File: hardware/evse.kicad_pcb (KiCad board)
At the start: 2 copper layers, 42.5 x 62.5 mm, 87 parts, among them J101 Boot, P101 CON-SENSOR2, P102 Relay, P104 12V/Motor/GP, P105 CP/PP/PE, U101 XMC1100, U102 PEM1-S12-D12-S, U103 MAX14850, U104 ADS1118I, U105 OPA171AIDBV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

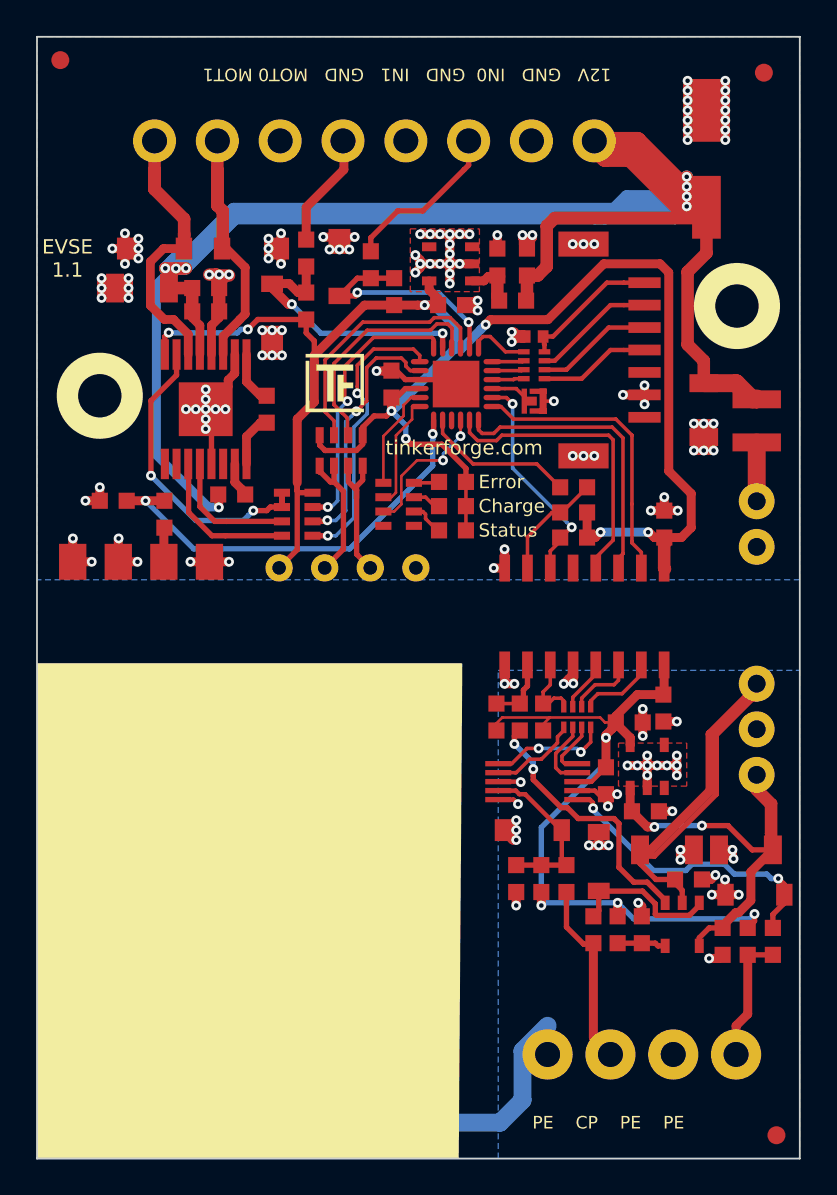
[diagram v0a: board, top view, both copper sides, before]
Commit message: fix tvs/zener diodes, fix pp description
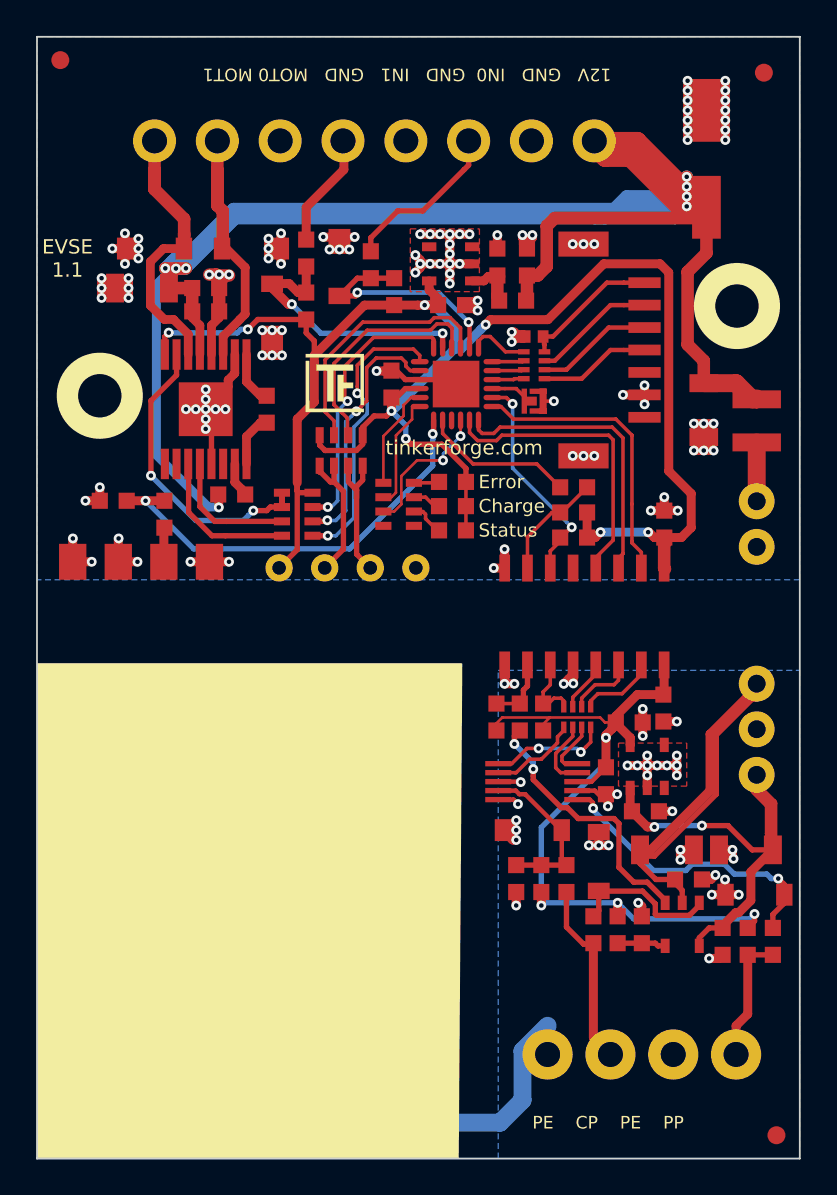
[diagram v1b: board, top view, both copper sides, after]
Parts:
- turned D104 to 270 degrees
- turned D106 to 180 degrees
- turned D107 to 180 degrees
- turned D110 to 90 degrees
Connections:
- D104 pad 1: INPUT-MOTOR-SWITCH -> GND
- D104 pad 2: GND -> INPUT-MOTOR-SWITCH
- D106 pad 1: Net-(D106-Pad1) -> AGND
- D106 pad 2: AGND -> Net-(D106-Pad2)
- D107 pad 1: Net-(D107-Pad1) -> AGND
- D107 pad 2: AGND -> Net-(D107-Pad2)
- D110 pad 1: INPUT-GP -> GND
- D110 pad 2: GND -> INPUT-GP
- R108 pad 1: Net-(D106-Pad1) -> Net-(D106-Pad2)
- R109 pad 1: Net-(D106-Pad1) -> Net-(D106-Pad2)
- R110 pad 2: Net-(D106-Pad1) -> Net-(D106-Pad2)
- R112 pad 2: Net-(D107-Pad1) -> Net-(D107-Pad2)
- U104 pad 4: Net-(D106-Pad1) -> Net-(D106-Pad2)
- U104 pad 6: Net-(D107-Pad1) -> Net-(D107-Pad2)
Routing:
- net Net-(D107-Pad2): track 0.00 -> 16.7 mm, vias 0 -> 2
- net Net-(D107-Pad1): track 16.7 -> 0.00 mm, vias 2 -> 0
- net Net-(D106-Pad2): track 0.00 -> 9.22 mm
- net Net-(D106-Pad1): track 9.22 -> 0.00 mm
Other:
- board text added: "PE CP PE PP"
- board text removed: "PE CP PE PE"

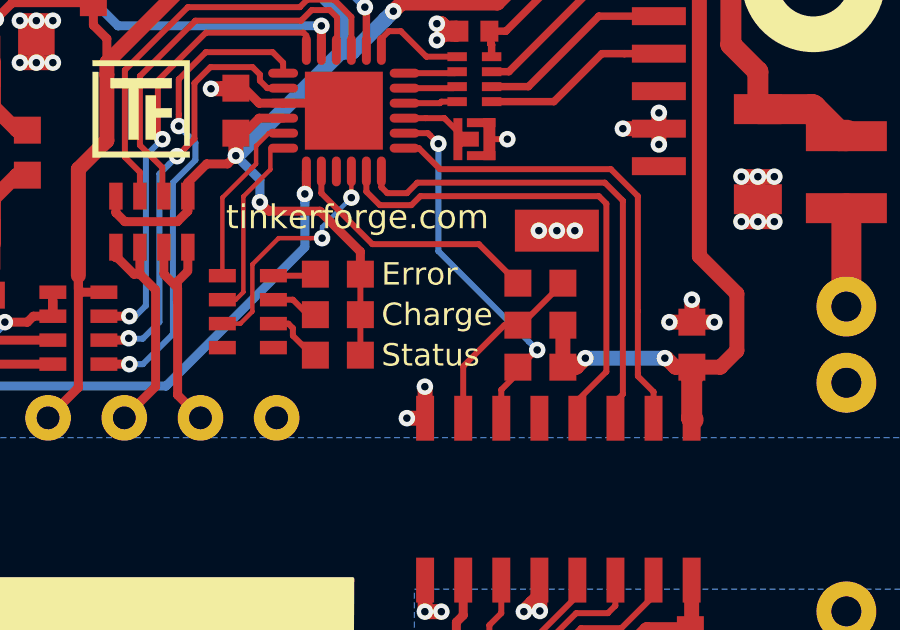
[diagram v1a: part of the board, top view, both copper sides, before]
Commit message: fix led colors and description
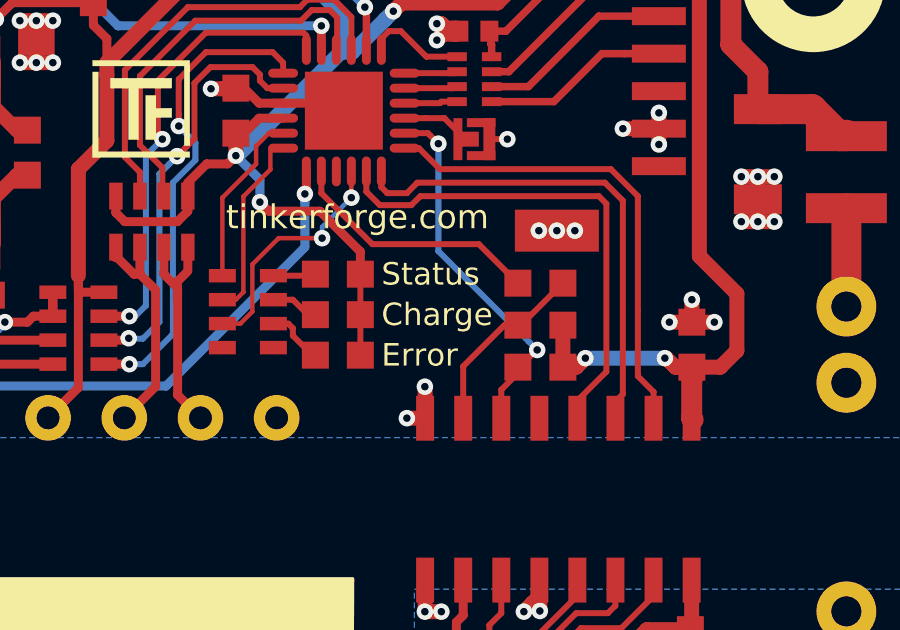
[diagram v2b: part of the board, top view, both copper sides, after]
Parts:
- D101: value blue -> red
- D103: value red -> blue
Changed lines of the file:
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@@
       (effects (font (size 0.2 0.2) (thickness 0.05)))
     )
-    (fp_text value blue (at 0.75 0.45) (layer F.Fab)
+    (fp_text value red (at 0.75 0.45) (layer F.Fab)
       (effects (font (size 0.2 0.2) (thickness 0.05)))
     )
@@
       (effects (font (size 0.2 0.2) (thickness 0.05)))
     )
-    (fp_text value red (at 0.75 0.45) (layer F.Fab)
+    (fp_text value blue (at 0.75 0.45) (layer F.Fab)
       (effects (font (size 0.2 0.2) (thickness 0.05)))
     )
@@
     (effects (font (size 0.8 0.8) (thickness 0.15)))
   )
-  (gr_text Error (at 163.6 81.95) (layer F.SilkS)
+  (gr_text Status (at 163.6 81.95) (layer F.SilkS)
     (effects (font (size 0.75 0.75) (thickness 0.15)) (justify left))
   )
@@
     (effects (font (size 0.75 0.75) (thickness 0.15)) (justify left))
   )
-  (gr_text Status (at 163.6 84.65) (layer F.SilkS)
+  (gr_text Error (at 163.6 84.65) (layer F.SilkS)
     (effects (font (size 0.75 0.75) (thickness 0.15)) (justify left))
   )
@@
   (segment (start 175.89996 105.55098) (end 175.350769 106.100171) (width 0.3) (layer F.Cu) (net 60))
   (segment (start 172.738202 104.75) (end 170.3 104.75) (width 0.3) (layer F.Cu) (net 60))
-  (segment (start 168.2383 101.35) (end 168.2383 102.9883) (width 0.25) (layer F.Cu) (net 87))
-  (segment (start 168.2383 102.9883) (end 168.5 103.25) (width 0.25) (layer F.Cu) (net 87))
-  (segment (start 165.7 103.3) (end 168.5 103.3) (width 0.3) (layer F.Cu) (net 87))
-  (segment (start 165.875998 99.350998) (end 166.200998 99.350998) (width 0.25) (layer F.Cu) (net 87))
-  (segment (start 165.675 99.15) (end 165.875998 99.350998) (width 0.25) (layer F.Cu) (net 87))
-  (segment (start 166.200998 99.350998) (end 168.2 101.35) (width 0.25) (layer F.Cu) (net 87))
-  (segment (start 164.7 99.15) (end 165.675 99.15) (width 0.25) (layer F.Cu) (net 87))
   (segment (start 162.6 73.375522) (end 162.6 74.5) (width 0.2) (layer F.Cu) (net 61))
   (segment (start 162.023479 72.799001) (end 162.6 73.375522) (width 0.2) (layer F.Cu) (net 61))
@@
   (segment (start 152.49 94.36) (end 153.251999 95.121999) (width 0.7) (layer F.Cu) (net 65))
   (segment (start 153.251999 95.121999) (end 153.251999 95.901999) (width 0.7) (layer F.Cu) (net 65))
-  (segment (start 180 106.05) (end 180.6 105.45) (width 0.3) (layer F.Cu) (net 86))
-  (segment (start 180 106.8) (end 180 106.05) (width 0.3) (layer F.Cu) (net 86))
-  (segment (start 180.6 105.45) (end 180.6 104.95) (width 0.3) (layer F.Cu) (net 86))
-  (segment (start 180.6383 104.95) (end 180.6383 104.3883) (width 0.3) (layer F.Cu) (net 86))
-  (via (at 180.3 104.05) (size 0.55) (drill 0.25) (layers F.Cu B.Cu) (net 86))
-  (segment (start 180.6383 104.3883) (end 180.574999 104.324999) (width 0.3) (layer F.Cu) (net 86))
-  (segment (start 180.574999 104.324999) (end 180.3 104.05) (width 0.3) (layer F.Cu) (net 86))
-  (via (at 169.985623 100.131499) (size 0.55) (drill 0.25) (layers F.Cu B.Cu) (net 86))
-  (segment (start 169.985623 100.028825) (end 169.985623 100.131499) (width 0.25) (layer F.Cu) (net 86))
-  (segment (start 169.975999 100.019201) (end 169.985623 100.028825) (width 0.25) (layer F.Cu) (net 86))
-  (segment (start 169.975999 99.825999) (end 169.975999 100.019201) (width 0.25) (layer F.Cu) (net 86))
-  (segment (start 169.1 99.65) (end 169.8 99.65) (width 0.25) (layer F.Cu) (net 86))
-  (segment (start 169.8 99.65) (end 169.975999 99.825999) (width 0.25) (layer F.Cu) (net 86))
-  (segment (start 170 100.25) (end 170 100.1) (width 0.3) (layer B.Cu) (net 86))
-  (segment (start 173.35 103.6) (end 170 100.25) (width 0.3) (layer B.Cu) (net 86))
-  (segment (start 175.15 103.6) (end 173.35 103.6) (width 0.3) (layer B.Cu) (net 86))
-  (segment (start 179.911092 104.05) (end 179.661092 103.8) (width 0.3) (layer B.Cu) (net 86))
-  (segment (start 179.661092 103.8) (end 177.85 103.8) (width 0.3) (layer B.Cu) (net 86))
-  (segment (start 175.5 103.25) (end 175.15 103.6) (width 0.3) (layer B.Cu) (net 86))
-  (segment (start 180.3 104.05) (end 179.911092 104.05) (width 0.3) (layer B.Cu) (net 86))
-  (segment (start 177.85 103.8) (end 177.3 103.25) (width 0.3) (layer B.Cu) (net 86))
-  (segment (start 177.3 103.25) (end 175.5 103.25) (width 0.3) (layer B.Cu) (net 86))
   (segment (start 164.75 70.5) (end 164.65 70.4) (width 0.7) (layer F.Cu) (net 68))
   (segment (start 163.24888 70.74996) (end 163.90004 70.74996) (width 0.5) (layer F.Cu) (net 68))
@@
   (via (at 161.62401 80.75) (size 0.55) (drill 0.25) (layers F.Cu B.Cu) (net 85))
   (segment (start 161.62401 80.37599) (end 161.62401 80.75) (width 0.15) (layer B.Cu) (net 85))
+  (segment (start 180 106.05) (end 180.6 105.45) (width 0.3) (layer F.Cu) (net 86))
+  (segment (start 180 106.8) (end 180 106.05) (width 0.3) (layer F.Cu) (net 86))
+  (segment (start 180.6 105.45) (end 180.6 104.95) (width 0.3) (layer F.Cu) (net 86))
+  (segment (start 180.6383 104.95) (end 180.6383 104.3883) (width 0.3) (layer F.Cu) (net 86))
+  (via (at 180.3 104.05) (size 0.55) (drill 0.25) (layers F.Cu B.Cu) (net 86))
+  (segment (start 180.6383 104.3883) (end 180.574999 104.324999) (width 0.3) (layer F.Cu) (net 86))
+  (segment (start 180.574999 104.324999) (end 180.3 104.05) (width 0.3) (layer F.Cu) (net 86))
+  (via (at 169.985623 100.131499) (size 0.55) (drill 0.25) (layers F.Cu B.Cu) (net 86))
+  (segment (start 169.985623 100.028825) (end 169.985623 100.131499) (width 0.25) (layer F.Cu) (net 86))
+  (segment (start 169.975999 100.019201) (end 169.985623 100.028825) (width 0.25) (layer F.Cu) (net 86))
+  (segment (start 169.975999 99.825999) (end 169.975999 100.019201) (width 0.25) (layer F.Cu) (net 86))
+  (segment (start 169.1 99.65) (end 169.8 99.65) (width 0.25) (layer F.Cu) (net 86))
+  (segment (start 169.8 99.65) (end 169.975999 99.825999) (width 0.25) (layer F.Cu) (net 86))
+  (segment (start 170 100.25) (end 170 100.1) (width 0.3) (layer B.Cu) (net 86))
+  (segment (start 173.35 103.6) (end 170 100.25) (width 0.3) (layer B.Cu) (net 86))
+  (segment (start 175.15 103.6) (end 173.35 103.6) (width 0.3) (layer B.Cu) (net 86))
+  (segment (start 179.911092 104.05) (end 179.661092 103.8) (width 0.3) (layer B.Cu) (net 86))
+  (segment (start 179.661092 103.8) (end 177.85 103.8) (width 0.3) (layer B.Cu) (net 86))
+  (segment (start 175.5 103.25) (end 175.15 103.6) (width 0.3) (layer B.Cu) (net 86))
+  (segment (start 180.3 104.05) (end 179.911092 104.05) (width 0.3) (layer B.Cu) (net 86))
+  (segment (start 177.85 103.8) (end 177.3 103.25) (width 0.3) (layer B.Cu) (net 86))
+  (segment (start 177.3 103.25) (end 175.5 103.25) (width 0.3) (layer B.Cu) (net 86))
+  (segment (start 168.2383 101.35) (end 168.2383 102.9883) (width 0.25) (layer F.Cu) (net 87))
+  (segment (start 168.2383 102.9883) (end 168.5 103.25) (width 0.25) (layer F.Cu) (net 87))
+  (segment (start 165.7 103.3) (end 168.5 103.3) (width 0.3) (layer F.Cu) (net 87))
+  (segment (start 165.875998 99.350998) (end 166.200998 99.350998) (width 0.25) (layer F.Cu) (net 87))
+  (segment (start 165.675 99.15) (end 165.875998 99.350998) (width 0.25) (layer F.Cu) (net 87))
+  (segment (start 166.200998 99.350998) (end 168.2 101.35) (width 0.25) (layer F.Cu) (net 87))
+  (segment (start 164.7 99.15) (end 165.675 99.15) (width 0.25) (layer F.Cu) (net 87))
   (zone (net 6) (net_name AGND) (layer B.Cu) (hatch edge 0.508)
     (connect_pads yes (clearance 0))

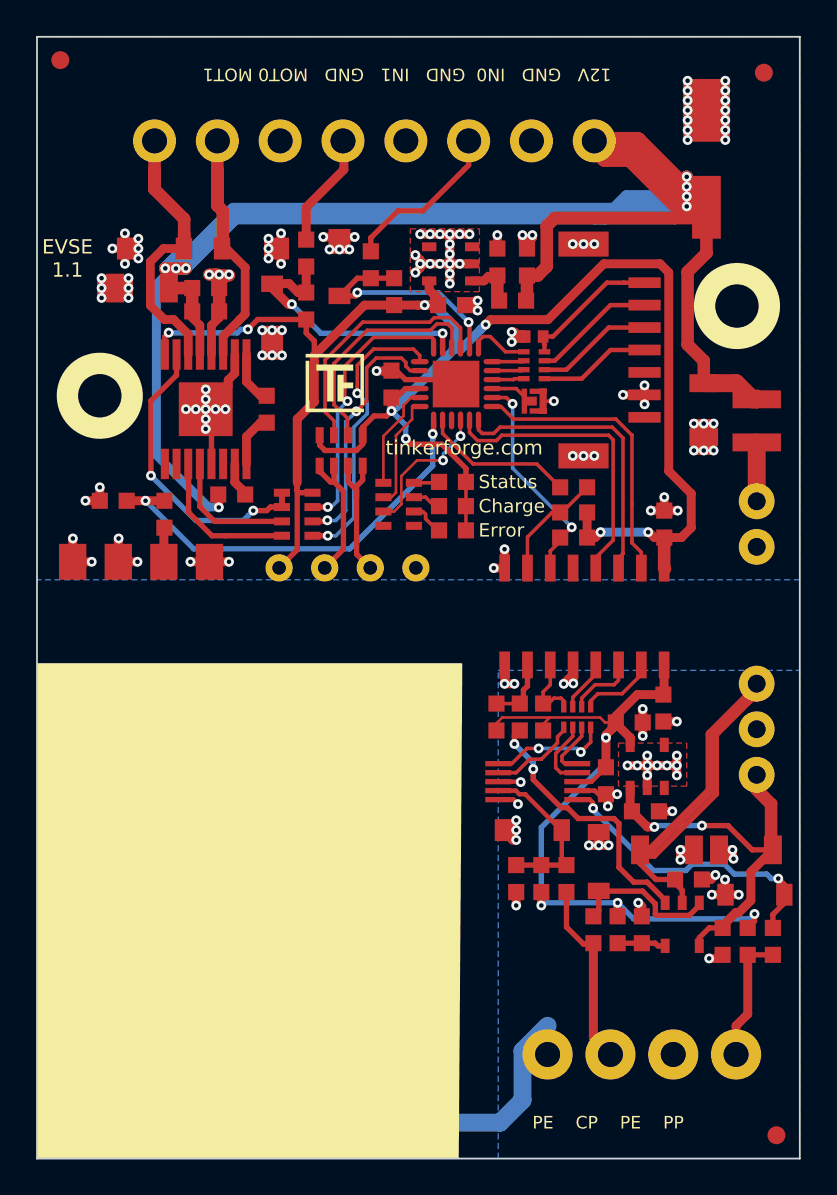
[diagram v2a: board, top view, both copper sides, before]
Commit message: add version 1.2:
remove error led
add maximum power jumper
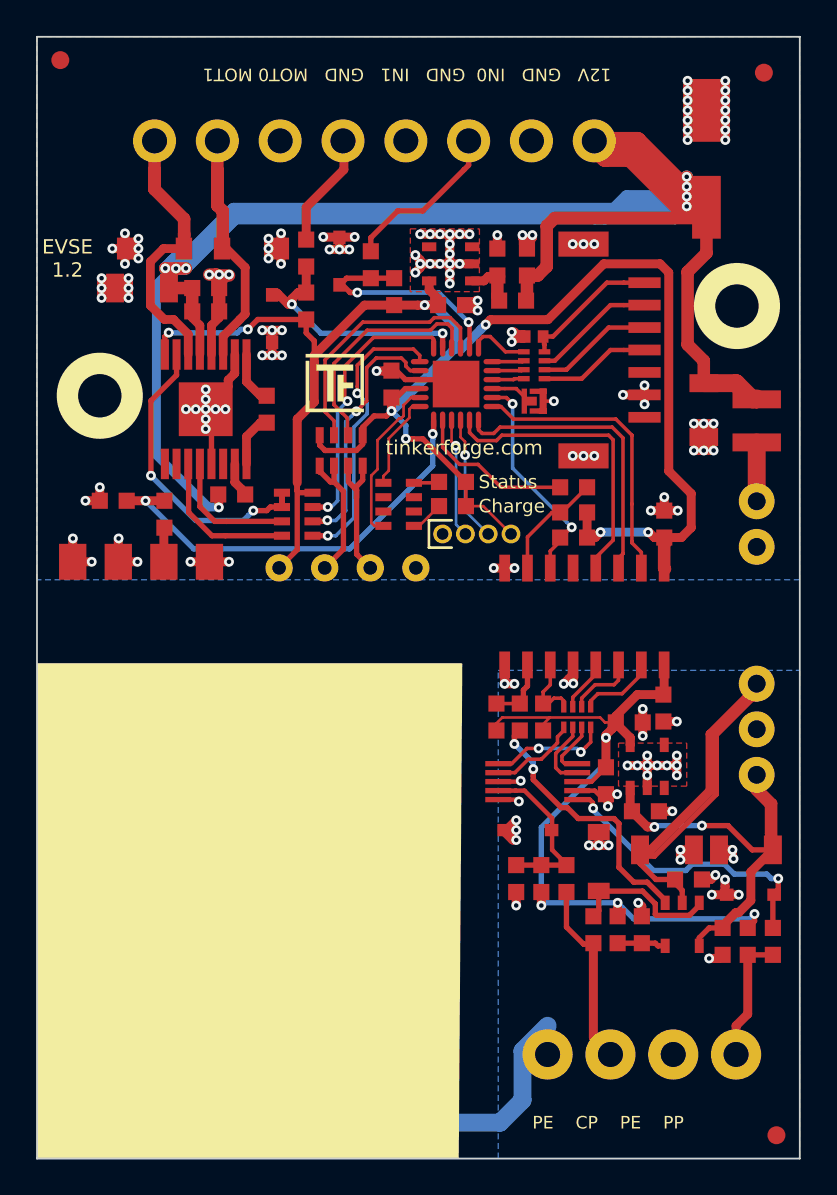
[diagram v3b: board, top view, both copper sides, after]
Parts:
- removed D101: red, kicad-libraries:D0603F
- added J102: Power Setting, kicad-libraries:Pin_Header_Straight_1x04_127, F.Cu at (161.6, 84.8)
- D104, D110: value SMF3.3 -> ‎PESD3V3L1BA; footprint kicad-libraries:SOD-123FL -> kicad-libraries:SOD-323
- D106, D107: value SMF4L5.0A -> ‎PESD5V0L1BA; footprint kicad-libraries:SOD-123FL -> kicad-libraries:SOD-323
- moved D104 0.30 mm to (152.1, 72.8), turned to 90 degrees
- moved D110 0.30 mm to (155.8, 69.7)
- moved D106 0.25 mm to (166.3, 101.3), turned to 0 degrees
- moved D107 0.25 mm to (178.8, 105.0), turned to 0 degrees
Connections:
- D110 pad 1: GND -> INPUT-GP
- D110 pad 2: INPUT-GP -> GND
- RP102 pad 2: LED_ERROR -> Net-(RP102-Pad2)
- RP102 pad 6: Net-(D102-Pad2) -> Net-(RP102-Pad6)
- RP102 pad 8: Net-(RP102-Pad8) -> Net-(D102-Pad2)
- U101 pad 11: Net-(RP102-Pad4) -> Net-(RP102-Pad1)
- U101 pad 12: Net-(RP102-Pad3) -> Net-(RP102-Pad4)
- U101 pad 16: LED_ERROR -> Net-(J102-Pad3)
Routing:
- net Net-(RP102-Pad1): track 0.00 -> 9.22 mm
- net LED_ERROR: track 8.06 -> 0.00 mm, vias 2 -> 0
- net Net-(J102-Pad3): track 0.00 -> 6.96 mm, vias 0 -> 1
- net Net-(J102-Pad2): track 0.00 -> 6.64 mm, vias 0 -> 1
- net Net-(RP102-Pad3): track 5.98 -> 0.00 mm
- net Net-(RP102-Pad7): track 2.44 -> 0.00 mm
- net 3V3: track 100.7 -> 102.1 mm
- net INPUT-MOTOR-SWITCH: track 15.3 -> 13.9 mm
- net Net-(RP102-Pad4): track 5.91 -> 5.36 mm
- net GND: track 93.7 -> 93.2 mm
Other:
- board text added: "Copyright Tinkerforge GmbH 2020. This documentation describes Open Hardware and is licensed under the CERN OHL v. 1.1. You may redistribute and modify this documentation under the terms of the CERN OHL v.1.1. (http://ohwr.org/cernohl). This documentation is distributed WITHOUT ANY EXPRESS OR IMPLIED WARRANTY, INCLUDING OF MERCHANTABILITY, SATISFACTORY QUALITY AND FITNESS FOR A PARTICULAR PURPOSE.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"
- board text added: "EVSE 1.2"
- board text removed: "EVSE 1.1"
- board text removed: "Error"
